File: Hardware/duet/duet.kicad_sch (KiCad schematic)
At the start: 0 parts

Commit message: Add RAM to kicad schematic
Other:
- added sheet FPGA Top (fpga_top.kicad_sch)
- added sheet RAM and Flash memory (ram_flash.kicad_sch)
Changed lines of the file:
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@@
 	(generator "eeschema")
 	(generator_version "10.0")
-	(paper "A4")
+	(paper "A3")
+	(sheet
+		(at 34.29 33.02)
+		(size 97.79 44.45)
+		(exclude_from_sim no)
+		(in_bom yes)
+		(on_board yes)
+		(dnp no)
+		(fields_autoplaced yes)
+		(stroke
+			(width 0.1524)
+			(type solid)
+		)
+		(fill
+			(color 0 0 0 0)
+		)
+		(property "Sheetname" "FPGA Top"
+			(at 34.29 32.3084 0)
+			(show_name no)
+			(do_not_autoplace no)
+			(effects
+				(font
+					(size 1.27 1.27)
+				)
+				(justify left bottom)
+			)
+		)
+		(property "Sheetfile" "fpga_top.kicad_sch"
+			(at 34.29 78.0546 0)
+			(show_name no)
+			(do_not_autoplace no)
+			(effects
+				(font
+					(size 1.27 1.27)
+				)
+				(justify left top)
+			)
+		)
+		(instances
+			(project "duet"
+				(path "/0eef67e7-bb51-4885-9085-a6db10d7906a"
+					(page "2")
+				)
+			)
+		)
+	)
+	(sheet
+		(at 147.32 34.29)
+		(size 55.88 33.02)
+		(exclude_from_sim no)
+		(in_bom yes)
+		(on_board yes)
+		(dnp no)
+		(fields_autoplaced yes)
+		(stroke
+			(width 0.1524)
+			(type solid)
+		)
+		(fill
+			(color 0 0 0 0)
+		)
+		(property "Sheetname" "RAM and Flash memory"
+			(at 147.32 33.5784 0)
+			(show_name no)
+			(do_not_autoplace no)
+			(effects
+				(font
+					(size 1.27 1.27)
+				)
+				(justify left bottom)
+			)
+		)
+		(property "Sheetfile" "ram_flash.kicad_sch"
+			(at 147.32 67.8946 0)
+			(show_name no)
+			(do_not_autoplace no)
+			(effects
+				(font
+					(size 1.27 1.27)
+				)
+				(justify left top)
+			)
+		)
+		(instances
+			(project "duet"
+				(path "/0eef67e7-bb51-4885-9085-a6db10d7906a"
+					(page "3")
+				)
+			)
+		)
+	)
 	(sheet_instances
 		(path "/"

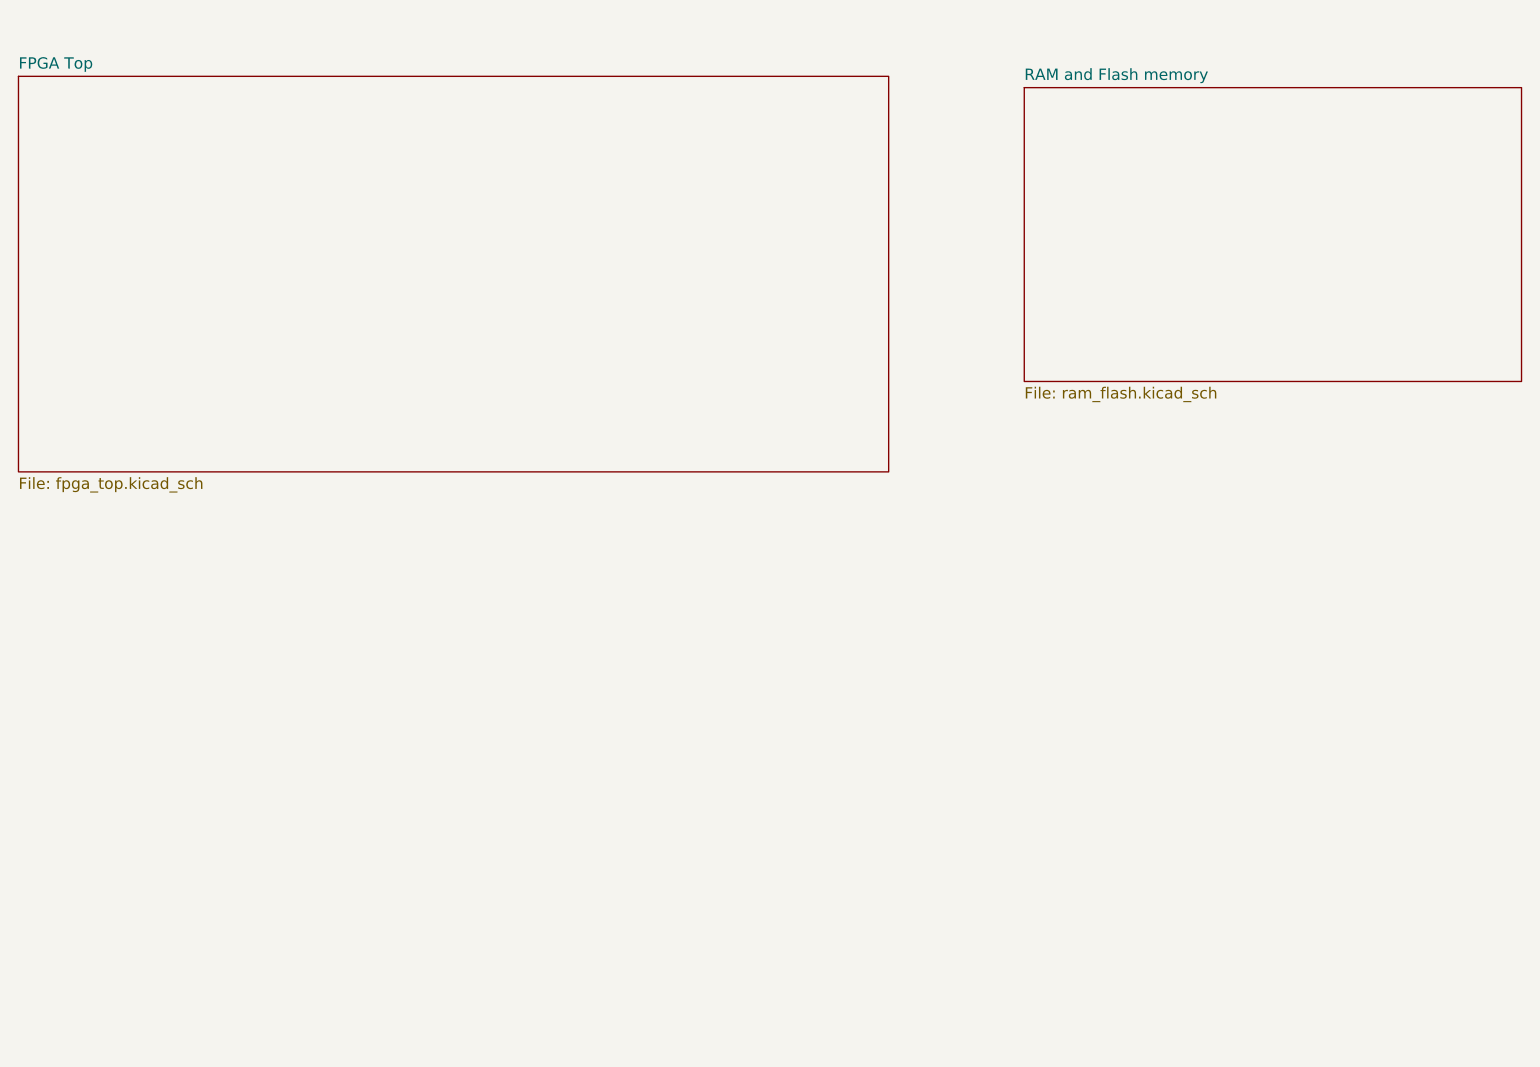
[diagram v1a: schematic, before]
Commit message: Add ECP5 configuration pins and labels
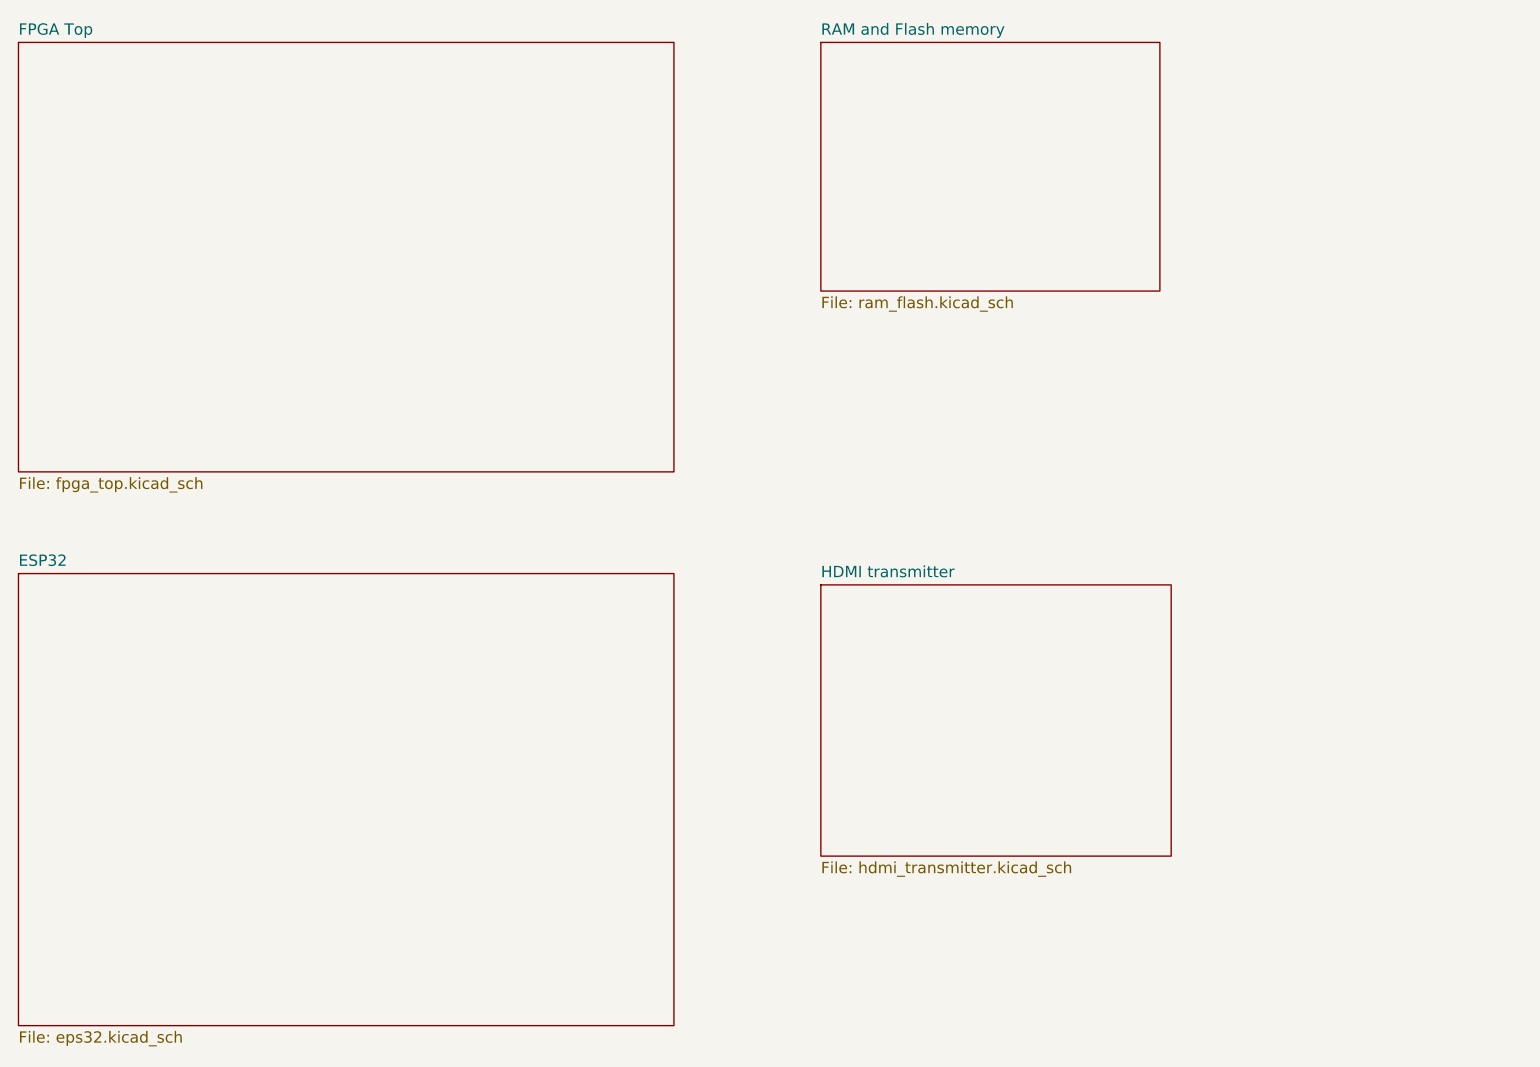
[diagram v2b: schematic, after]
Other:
- added sheet ESP32 (eps32.kicad_sch)
- added sheet HDMI transmitter (hdmi_transmitter.kicad_sch)
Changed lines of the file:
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@@
 	(paper "A3")
 	(sheet
-		(at 34.29 33.02)
-		(size 97.79 44.45)
+		(at 34.29 29.21)
+		(size 73.66 48.26)
 		(exclude_from_sim no)
 		(in_bom yes)
@@
 		)
 		(property "Sheetname" "FPGA Top"
-			(at 34.29 32.3084 0)
+			(at 34.29 28.4984 0)
 			(show_name no)
 			(do_not_autoplace no)
@@
 	)
 	(sheet
-		(at 147.32 34.29)
-		(size 55.88 33.02)
+		(at 34.29 88.9)
+		(size 73.66 50.8)
+		(exclude_from_sim no)
+		(in_bom yes)
+		(on_board yes)
+		(dnp no)
+		(fields_autoplaced yes)
+		(stroke
+			(width 0.1524)
+			(type solid)
+		)
+		(fill
+			(color 0 0 0 0)
+		)
+		(property "Sheetname" "ESP32"
+			(at 34.29 88.1884 0)
+			(show_name no)
+			(do_not_autoplace no)
+			(effects
+				(font
+					(size 1.27 1.27)
+				)
+				(justify left bottom)
+			)
+		)
+		(property "Sheetfile" "eps32.kicad_sch"
+			(at 34.29 140.2846 0)
+			(show_name no)
+			(do_not_autoplace no)
+			(effects
+				(font
+					(size 1.27 1.27)
+				)
+				(justify left top)
+			)
+		)
+		(instances
+			(project "duet"
+				(path "/0eef67e7-bb51-4885-9085-a6db10d7906a"
+					(page "4")
+				)
+			)
+		)
+	)
+	(sheet
+		(at 124.46 29.21)
+		(size 38.1 27.94)
 		(exclude_from_sim no)
 		(in_bom yes)
@@
 		)
 		(property "Sheetname" "RAM and Flash memory"
-			(at 147.32 33.5784 0)
+			(at 124.46 28.4984 0)
 			(show_name no)
 			(do_not_autoplace no)
@@
 		)
 		(property "Sheetfile" "ram_flash.kicad_sch"
-			(at 147.32 67.8946 0)
+			(at 124.46 57.7346 0)
 			(show_name no)
 			(do_not_autoplace no)
@@
 				)
 			)
+		)
+	)
+	(sheet
+		(at 124.46 90.17)
+		(size 39.37 30.48)
+		(exclude_from_sim no)
+		(in_bom yes)
+		(on_board yes)
+		(dnp no)
+		(fields_autoplaced yes)
+		(stroke
+			(width 0.1524)
+			(type solid)
+		)
+		(fill
+			(color 0 0 0 0)
+		)
+		(property "Sheetname" "HDMI transmitter"
+			(at 124.46 89.4584 0)
+			(show_name no)
+			(do_not_autoplace no)
+			(effects
+				(font
+					(size 1.27 1.27)
+				)
+				(justify left bottom)
+			)
+		)
+		(property "Sheetfile" "hdmi_transmitter.kicad_sch"
+			(at 124.46 121.2346 0)
+			(show_name no)
+			(do_not_autoplace no)
+			(effects
+				(font
+					(size 1.27 1.27)
+				)
+				(justify left top)
+			)
+		)
+		(instances
+			(project "duet"
+				(path "/0eef67e7-bb51-4885-9085-a6db10d7906a"
+					(page "5")
+				)
+			)

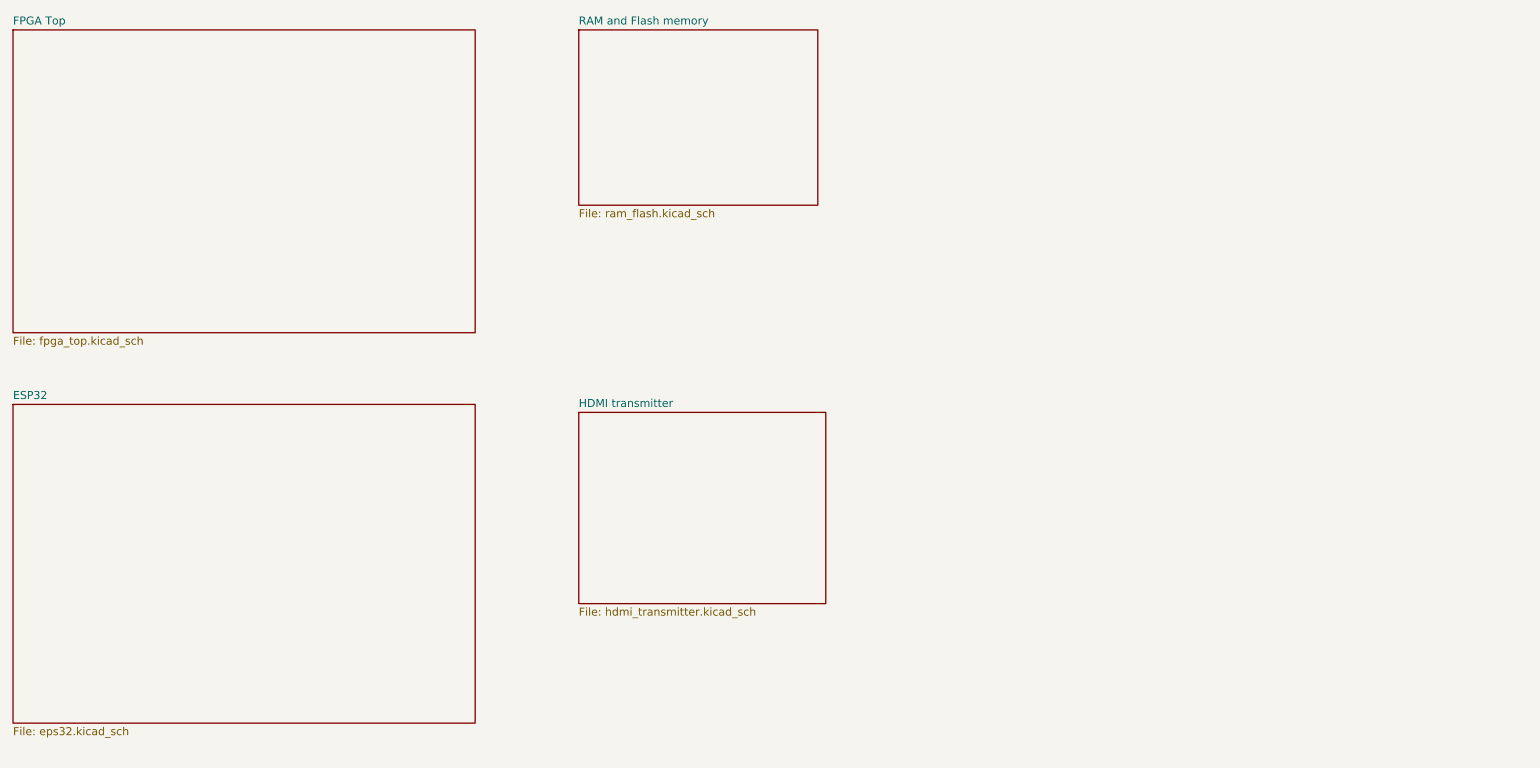
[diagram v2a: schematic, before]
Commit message: Adds HDMI transmitter and connector
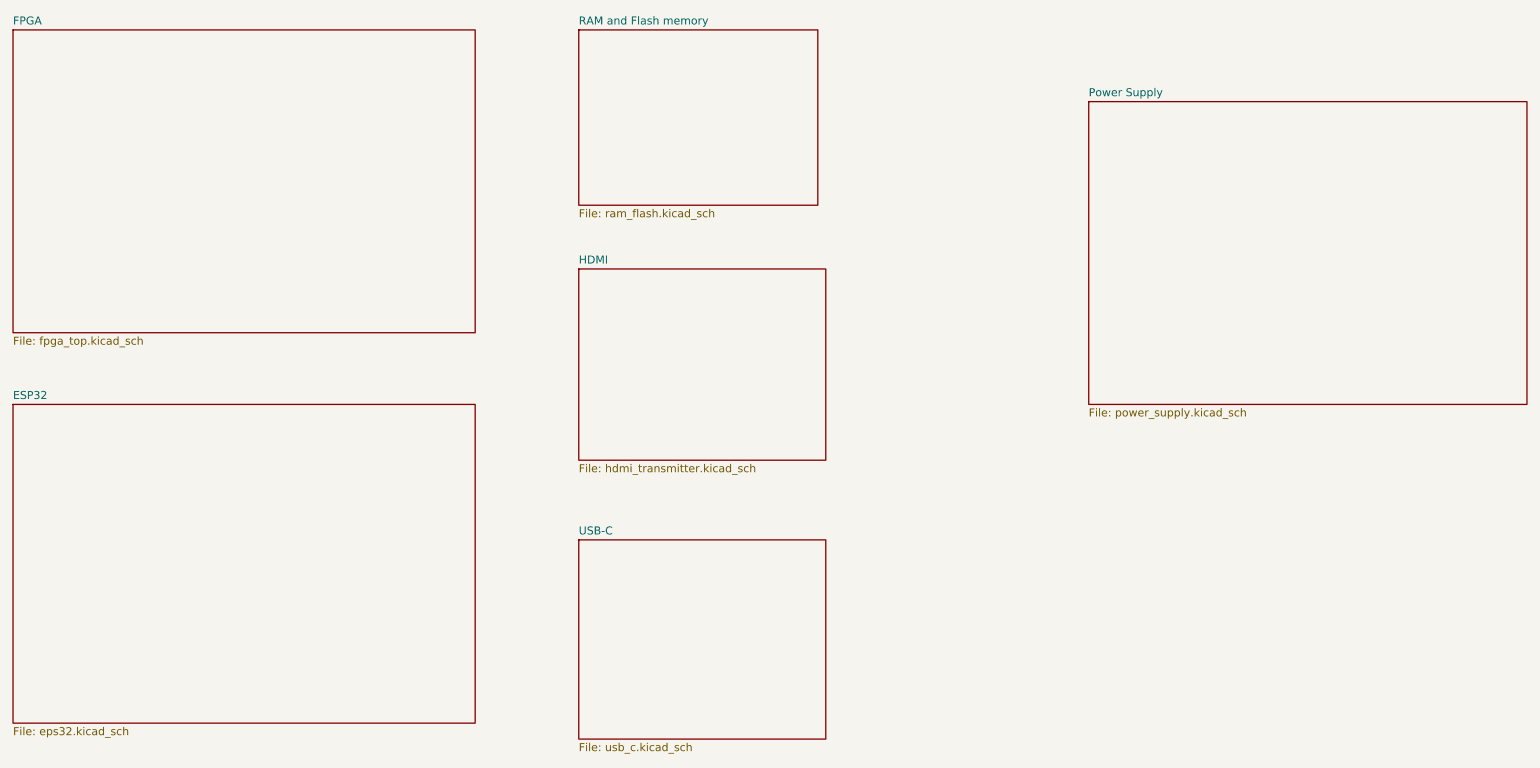
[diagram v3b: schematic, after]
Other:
- sheet FPGA Top renamed FPGA
- sheet HDMI transmitter renamed HDMI
- added sheet Power Supply (power_supply.kicad_sch)
- added sheet USB-C (usb_c.kicad_sch)
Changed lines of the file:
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@@
 			(color 0 0 0 0)
 		)
-		(property "Sheetname" "FPGA Top"
+		(property "Sheetname" "FPGA"
 			(at 34.29 28.4984 0)
 			(show_name no)
@@
 	)
 	(sheet
+		(at 205.74 40.64)
+		(size 69.85 48.26)
+		(exclude_from_sim no)
+		(in_bom yes)
+		(on_board yes)
+		(dnp no)
+		(fields_autoplaced yes)
+		(stroke
+			(width 0.1524)
+			(type solid)
+		)
+		(fill
+			(color 0 0 0 0)
+		)
+		(property "Sheetname" "Power Supply"
+			(at 205.74 39.9284 0)
+			(show_name no)
+			(do_not_autoplace no)
+			(effects
+				(font
+					(size 1.27 1.27)
+				)
+				(justify left bottom)
+			)
+		)
+		(property "Sheetfile" "power_supply.kicad_sch"
+			(at 205.74 89.4846 0)
+			(show_name no)
+			(do_not_autoplace no)
+			(effects
+				(font
+					(size 1.27 1.27)
+				)
+				(justify left top)
+			)
+		)
+		(instances
+			(project "duet"
+				(path "/0eef67e7-bb51-4885-9085-a6db10d7906a"
+					(page "6")
+				)
+			)
+		)
+	)
+	(sheet
 		(at 124.46 29.21)
 		(size 38.1 27.94)
@@
 	)
 	(sheet
-		(at 124.46 90.17)
+		(at 124.46 110.49)
+		(size 39.37 31.75)
+		(exclude_from_sim no)
+		(in_bom yes)
+		(on_board yes)
+		(dnp no)
+		(fields_autoplaced yes)
+		(stroke
+			(width 0.1524)
+			(type solid)
+		)
+		(fill
+			(color 0 0 0 0)
+		)
+		(property "Sheetname" "USB-C"
+			(at 124.46 109.7784 0)
+			(show_name no)
+			(do_not_autoplace no)
+			(effects
+				(font
+					(size 1.27 1.27)
+				)
+				(justify left bottom)
+			)
+		)
+		(property "Sheetfile" "usb_c.kicad_sch"
+			(at 124.46 142.8246 0)
+			(show_name no)
+			(do_not_autoplace no)
+			(effects
+				(font
+					(size 1.27 1.27)
+				)
+				(justify left top)
+			)
+		)
+		(instances
+			(project "duet"
+				(path "/0eef67e7-bb51-4885-9085-a6db10d7906a"
+					(page "7")
+				)
+			)
+		)
+	)
+	(sheet
+		(at 124.46 67.31)
 		(size 39.37 30.48)
 		(exclude_from_sim no)
@@
 			(color 0 0 0 0)
 		)
-		(property "Sheetname" "HDMI transmitter"
-			(at 124.46 89.4584 0)
+		(property "Sheetname" "HDMI"
+			(at 124.46 66.5984 0)
 			(show_name no)
 			(do_not_autoplace no)
@@
 		)
 		(property "Sheetfile" "hdmi_transmitter.kicad_sch"
-			(at 124.46 121.2346 0)
-			(show_name no)
-			(do_not_autoplace no)
+			(at 124.46 98.3746 0)
+			(show_name no)
+			(do_not_autoplace no)

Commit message: Adds ESP32 and pull up-down resistors
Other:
- removed sheet USB-C
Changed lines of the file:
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@@
-	)
-	(sheet
-		(at 124.46 110.49)
-		(size 39.37 31.75)
-		(exclude_from_sim no)
-		(in_bom yes)
-		(on_board yes)
-		(dnp no)
-		(fields_autoplaced yes)
-		(stroke
-			(width 0.1524)
-			(type solid)
-		)
-		(fill
-			(color 0 0 0 0)
-		)
-		(property "Sheetname" "USB-C"
-			(at 124.46 109.7784 0)
-			(show_name no)
-			(do_not_autoplace no)
-			(effects
-				(font
-					(size 1.27 1.27)
-				)
-				(justify left bottom)
-			)
-		)
-		(property "Sheetfile" "usb_c.kicad_sch"
-			(at 124.46 142.8246 0)
-			(show_name no)
-			(do_not_autoplace no)
-			(effects
-				(font
-					(size 1.27 1.27)
-				)
-				(justify left top)
-			)
-		)
-		(instances
-			(project "duet"
-				(path "/0eef67e7-bb51-4885-9085-a6db10d7906a"
-					(page "7")
-				)
-			)
-		)
 	)
 	(sheet
